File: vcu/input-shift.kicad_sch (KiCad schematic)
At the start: 15 parts, among them U5 HCF4010

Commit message: feat(vcu): update DRS servo voltage regulator to LM1804
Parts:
- renumbered C6 to C2, C7 to C3, TP13 to TP10, TP14 to TP11, TP12 to TP9, U5 to U4
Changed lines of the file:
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@@
   (symbol (lib_id "power:+3V3") (at 113.665 39.37 0) (unit 1)
     (in_bom yes) (on_board yes)
-    (property "Reference" "#PWR036" (id 0) (at 113.665 43.18 0)
+    (property "Reference" "#PWR033" (id 0) (at 113.665 43.18 0)
       (effects (font (size 1.27 1.27)) hide)
     )
@@
   (symbol (lib_id "power:GND") (at 44.45 93.98 0) (unit 1)
     (in_bom yes) (on_board yes)
-    (property "Reference" "#PWR028" (id 0) (at 44.45 100.33 0)
+    (property "Reference" "#PWR025" (id 0) (at 44.45 100.33 0)
       (effects (font (size 1.27 1.27)) hide)
     )
@@
   (symbol (lib_id "Connector:TestPoint_Small") (at 50.165 77.47 0) (unit 1)
     (in_bom yes) (on_board yes)
-    (property "Reference" "TP13" (id 0) (at 51.435 76.1999 0)
+    (property "Reference" "TP10" (id 0) (at 51.435 76.1999 0)
       (effects (font (size 1.27 1.27)) (justify left))
     )
@@
   (symbol (lib_id "power:GND") (at 53.34 128.27 0) (unit 1)
     (in_bom yes) (on_board yes)
-    (property "Reference" "#PWR032" (id 0) (at 53.34 134.62 0)
+    (property "Reference" "#PWR029" (id 0) (at 53.34 134.62 0)
       (effects (font (size 1.27 1.27)) hide)
     )
@@
   (symbol (lib_id "power:GND") (at 97.79 52.07 0) (mirror y) (unit 1)
     (in_bom yes) (on_board yes)
-    (property "Reference" "#PWR033" (id 0) (at 97.79 58.42 0)
+    (property "Reference" "#PWR030" (id 0) (at 97.79 58.42 0)
       (effects (font (size 1.27 1.27)) hide)
     )
@@
   (symbol (lib_id "Connector:TestPoint_Small") (at 50.165 43.815 0) (unit 1)
     (in_bom yes) (on_board yes)
-    (property "Reference" "TP12" (id 0) (at 51.435 42.5449 0)
+    (property "Reference" "TP9" (id 0) (at 51.435 42.5449 0)
       (effects (font (size 1.27 1.27)) (justify left))
     )
@@
   (symbol (lib_id "power:GND") (at 44.45 59.69 0) (unit 1)
     (in_bom yes) (on_board yes)
-    (property "Reference" "#PWR027" (id 0) (at 44.45 66.04 0)
+    (property "Reference" "#PWR024" (id 0) (at 44.45 66.04 0)
       (effects (font (size 1.27 1.27)) hide)
     )
@@
   (symbol (lib_id "symbols:HCF4010") (at 111.125 69.85 0) (unit 1)
     (in_bom yes) (on_board yes) (fields_autoplaced)
-    (property "Reference" "U5" (id 0) (at 113.1444 82.55 0)
+    (property "Reference" "U4" (id 0) (at 113.1444 82.55 0)
       (effects (font (size 1.27 1.27)) (justify left))
     )
@@
   (symbol (lib_id "Device:C_Small") (at 97.79 46.99 0) (mirror y) (unit 1)
     (in_bom yes) (on_board yes)
-    (property "Reference" "C6" (id 0) (at 95.25 45.72 0)
+    (property "Reference" "C2" (id 0) (at 95.25 45.72 0)
       (effects (font (size 1.27 1.27)) (justify left))
     )
@@
   (symbol (lib_id "power:GND") (at 44.45 127 0) (unit 1)
     (in_bom yes) (on_board yes)
-    (property "Reference" "#PWR029" (id 0) (at 44.45 133.35 0)
+    (property "Reference" "#PWR026" (id 0) (at 44.45 133.35 0)
       (effects (font (size 1.27 1.27)) hide)
     )
@@
   (symbol (lib_id "power:GND") (at 111.125 85.09 0) (unit 1)
     (in_bom yes) (on_board yes)
-    (property "Reference" "#PWR035" (id 0) (at 111.125 91.44 0)
+    (property "Reference" "#PWR032" (id 0) (at 111.125 91.44 0)
       (effects (font (size 1.27 1.27)) hide)
     )
@@
   (symbol (lib_id "power:GND") (at 124.46 52.07 0) (unit 1)
     (in_bom yes) (on_board yes)
-    (property "Reference" "#PWR037" (id 0) (at 124.46 58.42 0)
+    (property "Reference" "#PWR034" (id 0) (at 124.46 58.42 0)
       (effects (font (size 1.27 1.27)) hide)
     )
@@
   (symbol (lib_id "power:+12V") (at 108.585 39.37 0) (unit 1)
     (in_bom yes) (on_board yes)
-    (property "Reference" "#PWR034" (id 0) (at 108.585 43.18 0)
+    (property "Reference" "#PWR031" (id 0) (at 108.585 43.18 0)
       (effects (font (size 1.27 1.27)) hide)
     )
@@
   (symbol (lib_id "power:GND") (at 53.34 60.96 0) (unit 1)
     (in_bom yes) (on_board yes)
-    (property "Reference" "#PWR030" (id 0) (at 53.34 67.31 0)
+    (property "Reference" "#PWR027" (id 0) (at 53.34 67.31 0)
       (effects (font (size 1.27 1.27)) hide)
     )
@@
   (symbol (lib_id "Device:C_Small") (at 124.46 46.99 0) (unit 1)
     (in_bom yes) (on_board yes)
-    (property "Reference" "C7" (id 0) (at 127 45.72 0)
+    (property "Reference" "C3" (id 0) (at 127 45.72 0)
       (effects (font (size 1.27 1.27)) (justify left))
     )
@@
   (symbol (lib_id "power:GND") (at 53.34 93.98 0) (unit 1)
     (in_bom yes) (on_board yes)
-    (property "Reference" "#PWR031" (id 0) (at 53.34 100.33 0)
+    (property "Reference" "#PWR028" (id 0) (at 53.34 100.33 0)
       (effects (font (size 1.27 1.27)) hide)
     )
@@
   (symbol (lib_id "Connector:TestPoint_Small") (at 50.165 111.76 0) (unit 1)
     (in_bom yes) (on_board yes)
-    (property "Reference" "TP14" (id 0) (at 51.435 110.4899 0)
-      (effects (font (size 1.27 1.27)) (justify left))
-    )
+    (property "Reference" "TP11" (id 0) (at 51.435 110.4899 0)
+      (effects (font (size 1.27 1.27)) (justify left))
+    )

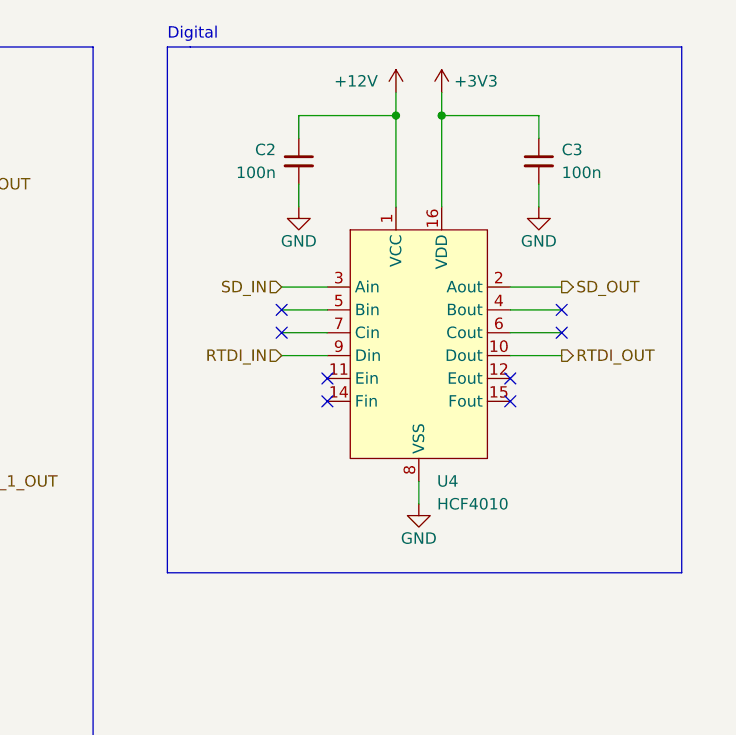
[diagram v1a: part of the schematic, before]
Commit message: feat(vcu): add spare inputs to input level shifter
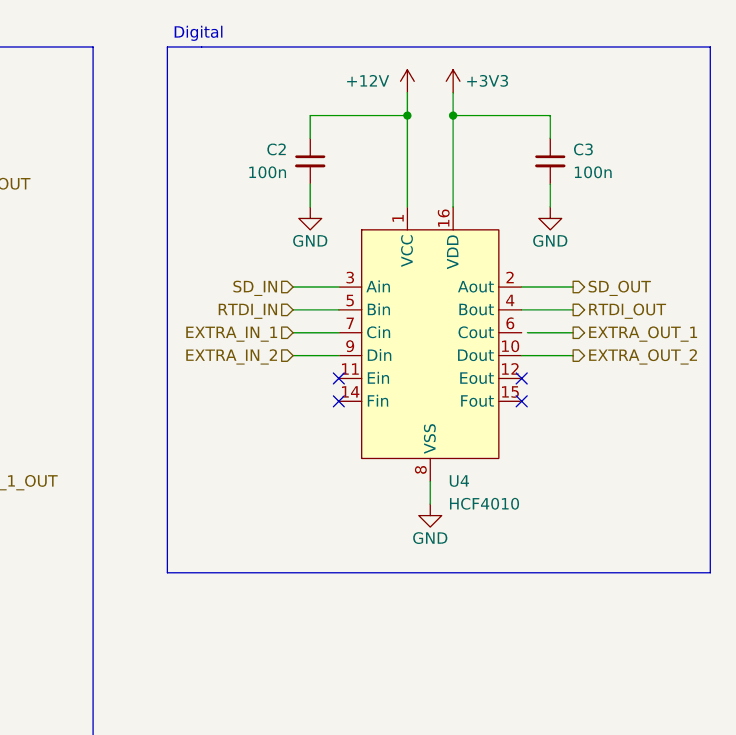
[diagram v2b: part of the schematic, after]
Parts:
- U4: Farnell 3132553 -> (none); Order Code (none) -> 511-HCF4010YM013TR; Supplier (none) -> Mouser
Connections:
- net RTDI_IN: now also U4.5 (Bin); no longer U4.9 (Din)
- net RTDI_OUT: now also U4.4 (Bout); no longer U4.10 (Dout)
- net EXTRA_IN_1: now reaches U4.7 (Cin)
- new net EXTRA_IN_2: U4.9 (Din)
- new net EXTRA_OUT_2: U4.10 (Dout)
- no-connect marks 8 -> 4
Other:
- moved on the sheet: C2, C3, U4

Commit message: fix(vcu): solve ERC errors caused by missing pin types
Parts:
- removed U4: HCF4010, Package_SO:SOIC-16_3.9x9.9mm_P1.27mm, symbol symbols:HCF4010
- added U4: HCF4010, Package_SO:SOIC-16_3.9x9.9mm_P1.27mm, symbol SUFST:HCF4010
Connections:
- net +12V: now also U4.1 (VCC)
- net +3V3: now also U4.16 (VDD)
- net EXTRA_IN_1: now also U4.7 (Cin)
- net EXTRA_IN_2: now also U4.9 (Din)
- net EXTRA_OUT_1: now also U4.6 (Cout)
- net EXTRA_OUT_2: now also U4.10 (Dout)
- net GND: now also U4.8 (VSS)
- net RTDI_IN: now also U4.5 (Bin)
- net RTDI_OUT: now also U4.4 (Bout)
- net SD_IN: now also U4.3 (Ain)
- net SD_OUT: now also U4.2 (Aout)

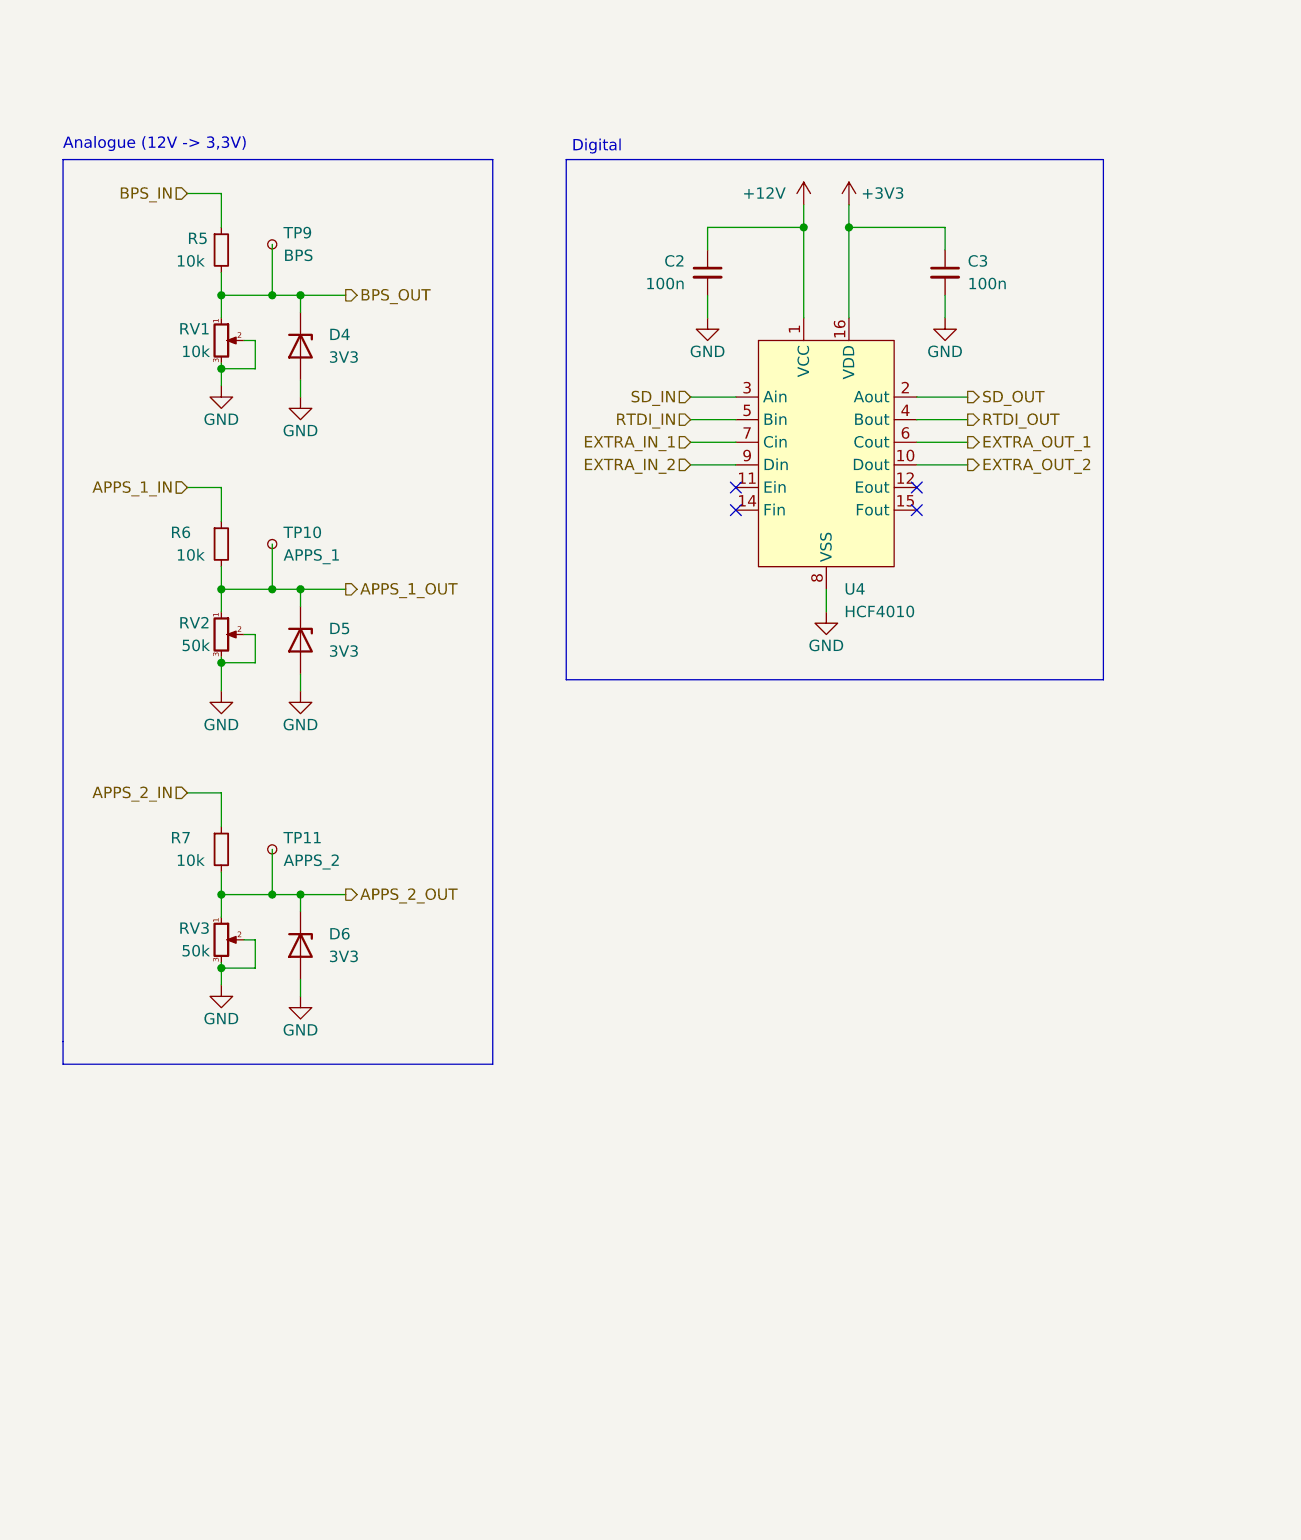
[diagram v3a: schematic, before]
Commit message: feat(vcu): final draft of schematic (#18)
* feat(vcu): add shutdown pin

* feat(lib): add FDN359BN MOSFET symbol

* feat(vcu): add variable resistor and new MOSFET to speaker driver

* fix(vcu): annotate MCU pins with text instead of labels

fixes about 80 ERC warnings

* fix(vcu): add exception to ERC for RTDS+ / 12V connection

* fix(vcu): remove PWR_FLAG from DRS regulator

* feat(vcu): add optional pull up resistors to set I2C bus time constant

* feat(lib): add TSSOP-8_3x6.4mm_P0.65mm footprint and 3D model

* feat(vcu): update EEPROM model and footprint

* feat(vcu): add 3.3V power connections from MCU

* feat(vcu): remove old indicator LEDs

can use those built in for dev board

* feat(vcu): add fixed resistor to analog input shift

* feat(vcu): remove green LED output from MCU

* fix(vcu): add missing footprints for MCU connectors

* fix(vcu): fix duplicate labels on CAN output connector

* fix(vcu): fix +12V and RTDS+ net connection error with net tie

* fix(lib): add missing body fills

* refactor(vcu): rename +3.3V net to +3V3

* feat(vcu): move DNP indication to separate field for I2C pullups

* refactor(vcu): rotate ground labels in MCU sheet

* refactor(vcu): clarify decoupling capacitor locations

* chore: remove old footprints folder

* feat(vcu): add optional split terminations to CAN transceivers

* chore: add SUFST sheet layout

* docs: add note about sheet layout to README

* feat(vcu): apply SUFST sheet layout

* feat(vcu): add spare GPIOs to MCU

* feat(vcu): change DRS regulator output cap to aluminium

* feat(vcu): add new signals to output connectors

* refactor(vcu): move analogue input shift out of subsheet

* feat(vcu): update input level shifter resistor values

* feat(lib): add MC14504BDG level shifter symbol

* feat(lib): add ILD615 symbol

* feat(vcu): change input level shifter to optocoupler based design

* feat(lib): add SN74LV1T125 symbol

* feat(vcu): updat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
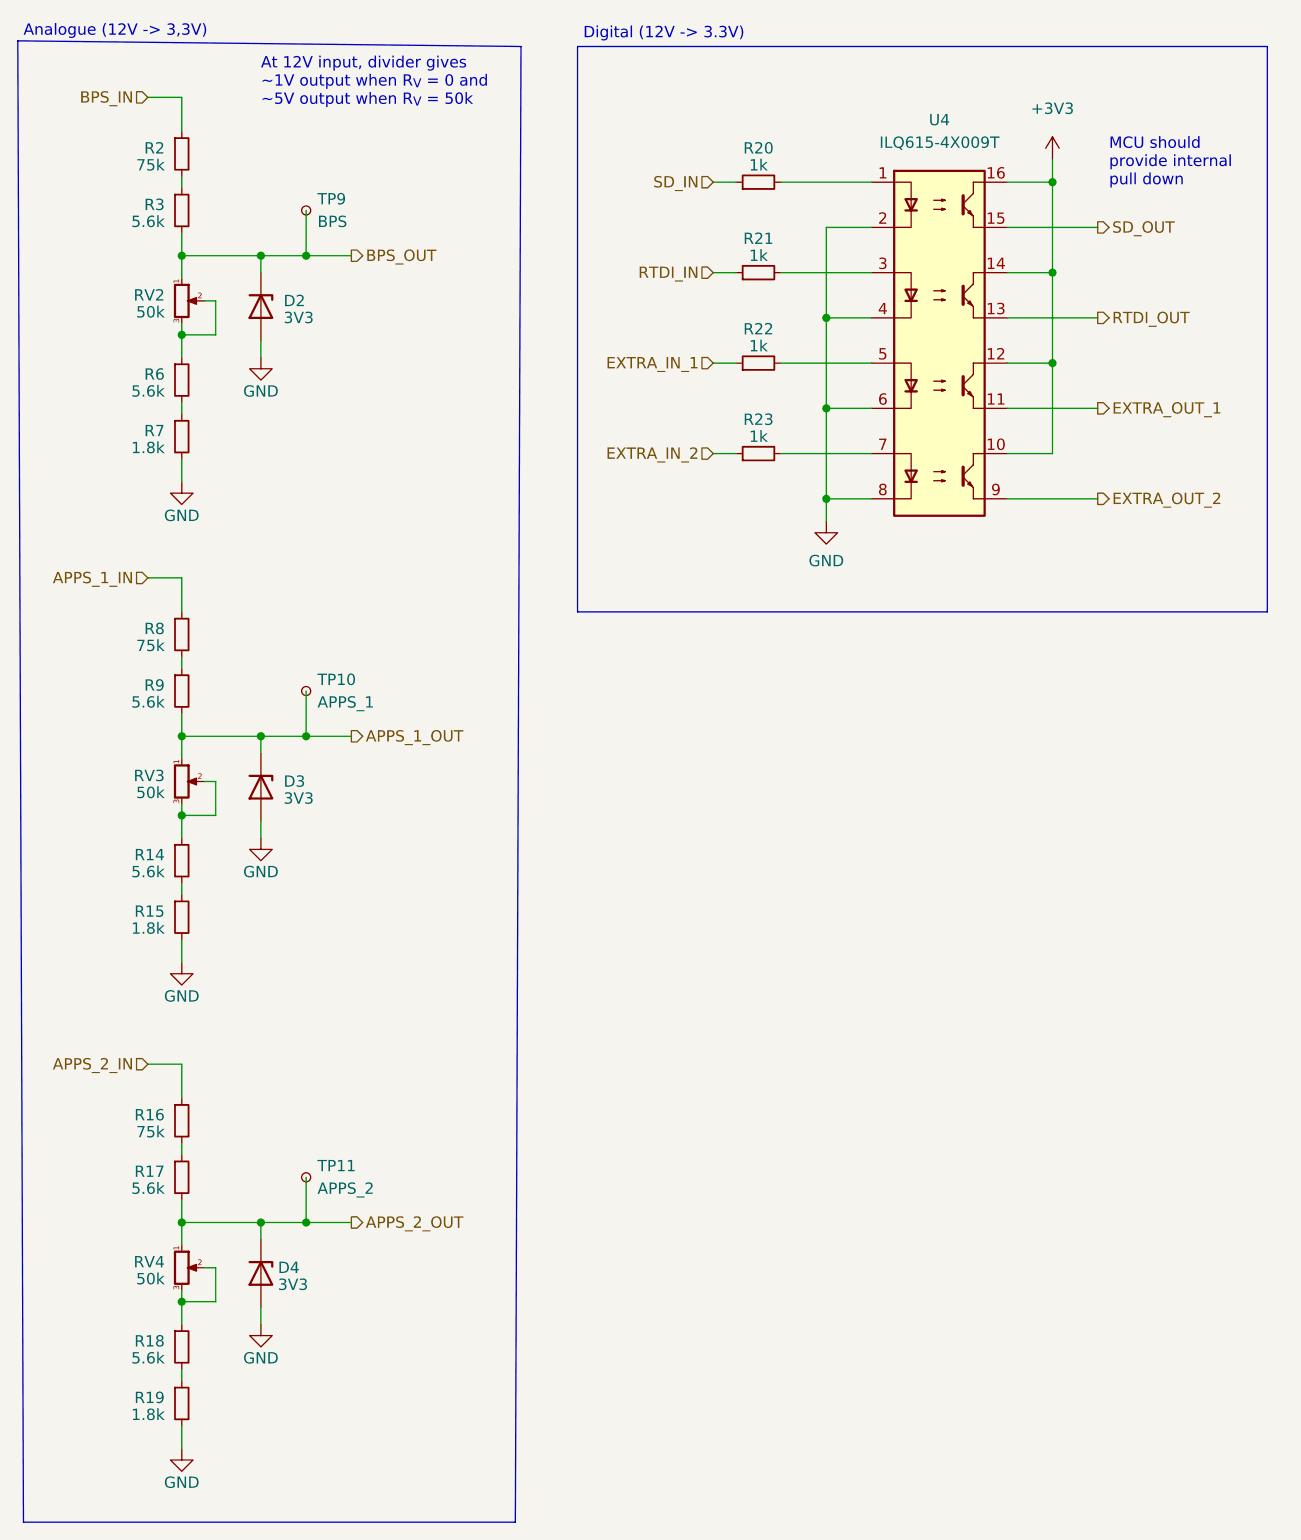
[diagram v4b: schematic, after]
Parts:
- removed C2, C3: 100n, Capacitor_SMD:C_0603_1608Metric_Pad1.08x0.95mm_HandSolder, symbol Device:C_Small
- removed D5, D6: 3V3, Package_TO_SOT_SMD:SOT-23, symbol Diode:BZX84Cxx
- removed R5: 10k, Resistor_SMD:R_0603_1608Metric_Pad0.98x0.95mm_HandSolder, symbol Device:R_Small
- removed RV1: 10k, Potentiometer_THT:Potentiometer_Vishay_T73XW_Horizontal, symbol Device:R_Potentiometer_Small
- removed U4: HCF4010, Package_SO:SOIC-16_3.9x9.9mm_P1.27mm, symbol SUFST:HCF4010
- added D2, D3: 3V3, Package_TO_SOT_SMD:SOT-23, symbol Diode:BZX84Cxx
- added R14, R17, R18, R3, R9: 5.6k, Resistor_SMD:R_0603_1608Metric_Pad0.98x0.95mm_HandSolder, symbol Device:R_Small
- added R15, R19: 1.8k, Resistor_SMD:R_0603_1608Metric_Pad0.98x0.95mm_HandSolder, symbol Device:R_Small
- added R16, R2, R8: 75k, Resistor_SMD:R_0603_1608Metric_Pad0.98x0.95mm_HandSolder, symbol Device:R_Small
- added R20, R21, R22, R23: 1k, symbol Device:R_Small
- added RV4: 50k, Potentiometer_THT:Potentiometer_Vishay_T73XW_Horizontal, symbol Device:R_Potentiometer_Small
- added U4: ILQ615-4X009T, symbol SUFST:ILQ615-4X009T
- R6: value 10k -> 5.6k
- R7: value 10k -> 1.8k
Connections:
- net +3V3: now also U4.10, U4.12, U4.14, U4.16
- net APPS_1_IN: now also R8.1; no longer R6.1
- net APPS_1_OUT: now also RV3.1, D3.3 (K), R9.2; no longer R6.2, RV2.1
- net APPS_2_IN: now also R16.1; no longer R7.1
- net APPS_2_OUT: now also D4.3 (K), R17.2, RV4.1; no longer R7.2, RV3.1
- net BPS_IN: now also R2.1
- net BPS_OUT: now also RV2.1, D2.3 (K), R3.2; no longer D4.3 (K)
- net EXTRA_IN_1: now also R22.1
- net EXTRA_IN_2: now also R23.1
- net EXTRA_OUT_1: now also U4.11
- net EXTRA_OUT_2: now also U4.9
- net GND: now also R7.2, D2.1 (A), D3.1 (A), R15.2, R19.2, U4.2, U4.4, U4.6, U4.8; no longer RV2.2, RV2.3, RV3.2, RV3.3
- net RTDI_IN: now also R21.1
- net RTDI_OUT: now also U4.13
- net SD_IN: now also R20.1
- net SD_OUT: now also U4.15
- new net: R14.2, R15.1
- new net: R18.1, RV4.2, RV4.3
- new net: R18.2, R19.1
- new net: R14.1, RV3.2, RV3.3
- new net: R22.2, U4.5
- new net: R2.2, R3.1
- new net: R6.1, RV2.2, RV2.3
- new net: R6.2, R7.1
- new net: R8.2, R9.1
- new net: R16.2, R17.1
- new net: R23.2, U4.7
- new net: R20.2, U4.1
- new net: R21.2, U4.3
- no-connect marks 4 -> 0
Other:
- note added: "At 12V input, divider gives ~1V output when R_{V} = 0 and ~5V output when R_{V} = 50k"
- note added: "Digital (12V -> 3.3V)"
- note added: "MCU should provide internal pull down"
- note removed: "Digital"
- moved on the sheet: TP10, TP11, TP9
